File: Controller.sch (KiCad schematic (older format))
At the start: 16 parts, among them IC1 SN74HCT245PWR, J1 RGB_3_pin, J2 RGB_3_pin, J3 RGB_3_pin, J4 RGB_3_pin, J5 RGB_3_pin, J6 RGB_3_pin, J7 RGB_3_pin, J8 RGB_3_pin, J9 AMP_Mate-N-Lok_Power, U1 ESP32_DevKit_V1_DOIT

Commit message: Rename project and create manufacturing files.
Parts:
- C1: footprint Capacitor_SMD:C_0603_1608Metric_Pad1.08x0.95mm_HandSolder -> Capacitor_SMD:C_0603_1608Metric
- IC1: footprint local:SN74HCT245PWR -> Package_SO:TSSOP-20_4.4x6.5mm_P0.65mm
- J9: footprint local:TE_MATE-N-LOK_350211-1_1x04_P5.08mm_Vertical -> Connector_TE-Connectivity:TE_MATE-N-LOK_1-794374-x_1x01_P4.14mm_Horizontal
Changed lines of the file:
@@
 F 0 "J9" H 4028 1446 50  0000 L CNN
 F 1 "AMP_Mate-N-Lok_Power" H 4028 1355 50  0000 L CNN
-F 2 "local:TE_MATE-N-LOK_350211-1_1x04_P5.08mm_Vertical" H 4050 1650 50  0001 L CNN
+F 2 "Connector_TE-Connectivity:TE_MATE-N-LOK_1-794374-x_1x01_P4.14mm_Horizontal" H 4050 1650 50  0001 L CNN
 F 3 "http://uk.rs-online.com/web/p/products/0471430" H 4050 1550 50  0001 L CNN
 F 4 "Pin & Socket Connectors CONN PCM 4 POS TIN" H 4050 1450 50  0001 L CNN "Description"
@@
 F 0 "C1" V 3921 3950 50  0000 C CNN
 F 1 "100nF" V 4012 3950 50  0000 C CNN
-F 2 "Capacitor_SMD:C_0603_1608Metric_Pad1.08x0.95mm_HandSolder" H 4150 3950 50  0001 C CNN
+F 2 "Capacitor_SMD:C_0603_1608Metric" H 4150 3950 50  0001 C CNN
 F 3 "~" H 4150 3950 50  0001 C CNN
 	1    4150 3950
@@
 Wire Wire Line
 	4650 4050 4650 4400
-Wire Bus Line
-	5000 2800 5000 5800
-Wire Bus Line
-	3250 3850 3250 5700
 $Comp
 L local:SN74HCT245PWR IC1
@@
 F 0 "IC1" H 4150 4665 50  0000 C CNN
 F 1 "SN74HCT245PWR" H 4150 4574 50  0000 C CNN
-F 2 "local:SN74HCT245PWR" H 4500 4500 50  0001 L CNN
+F 2 "Package_SO:TSSOP-20_4.4x6.5mm_P0.65mm" H 4500 4500 50  0001 L CNN
 F 3 "http://www.ti.com/general/docs/suppproductinfo.tsp?distId=10&gotoUrl=http%3A%2F%2Fwww.ti.com%2Flit%2Fgpn%2Fsn74hct245" H 4500 4400 50  0001 L CNN
 F 4 "Octal Bus Transceivers With 3-State Outputs" H 4500 4300 50  0001 L CNN "Description"
@@
 	1    0    0    -1
 $EndComp
+Wire Bus Line
+	5000 2800 5000 5800
+Wire Bus Line
+	3250 3850 3250 5700
 $EndSCHEMATC

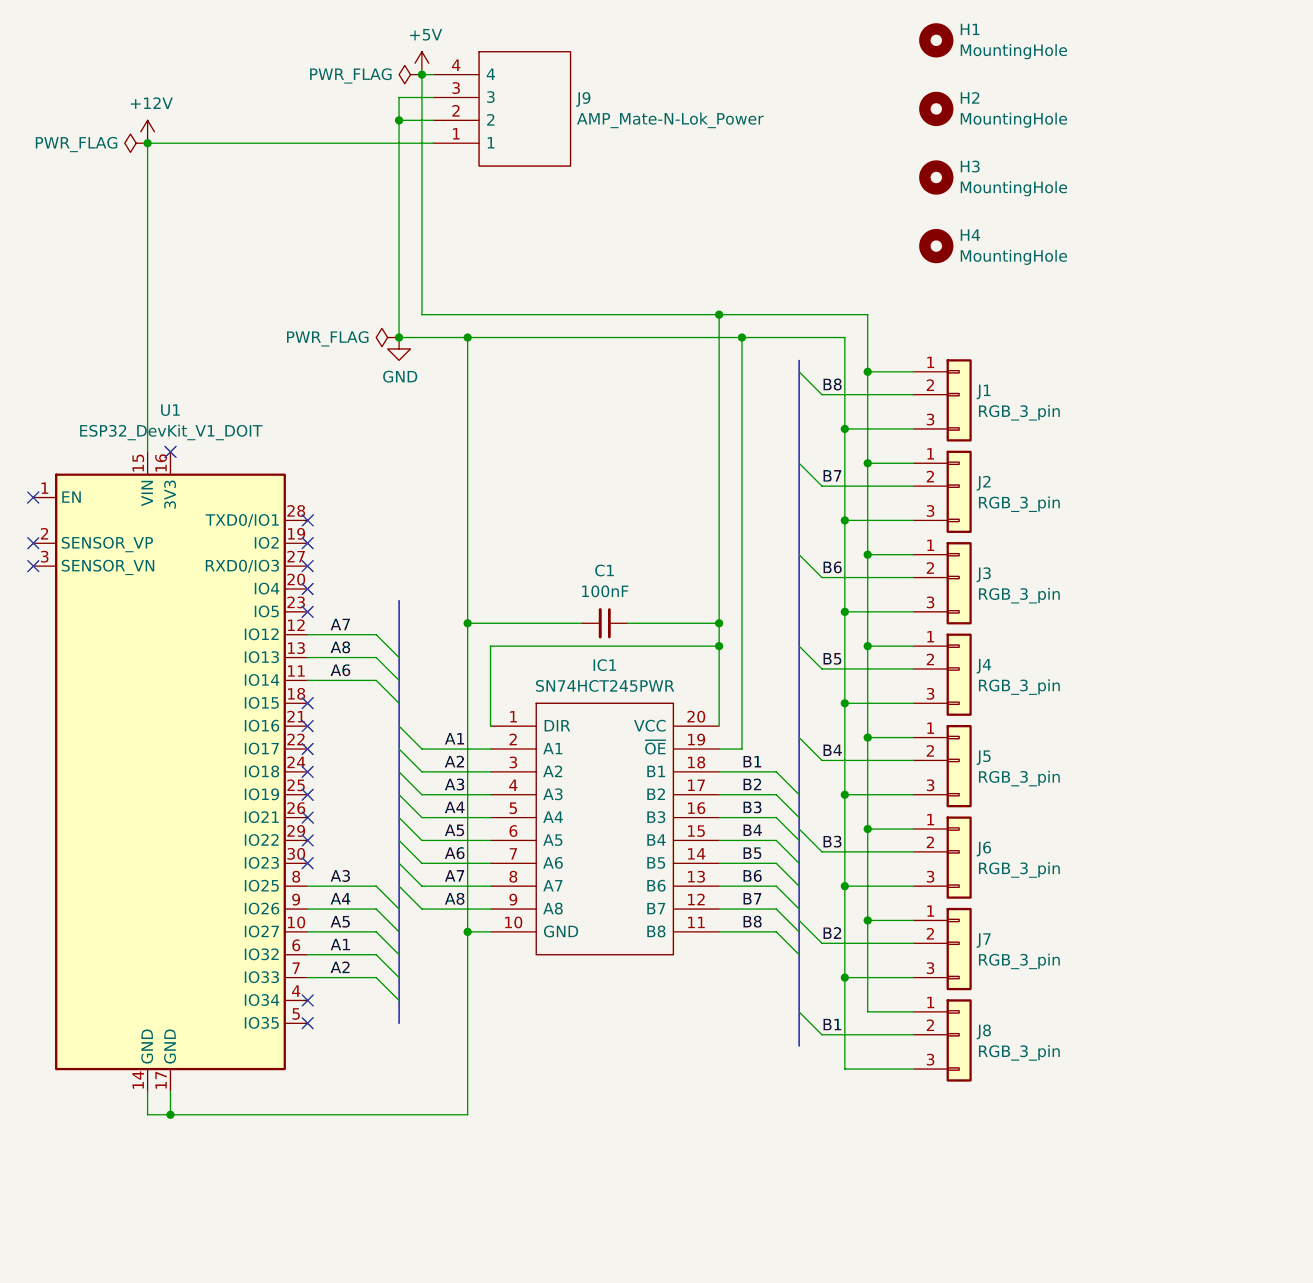
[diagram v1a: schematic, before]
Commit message: More compact layout with 10 channels.
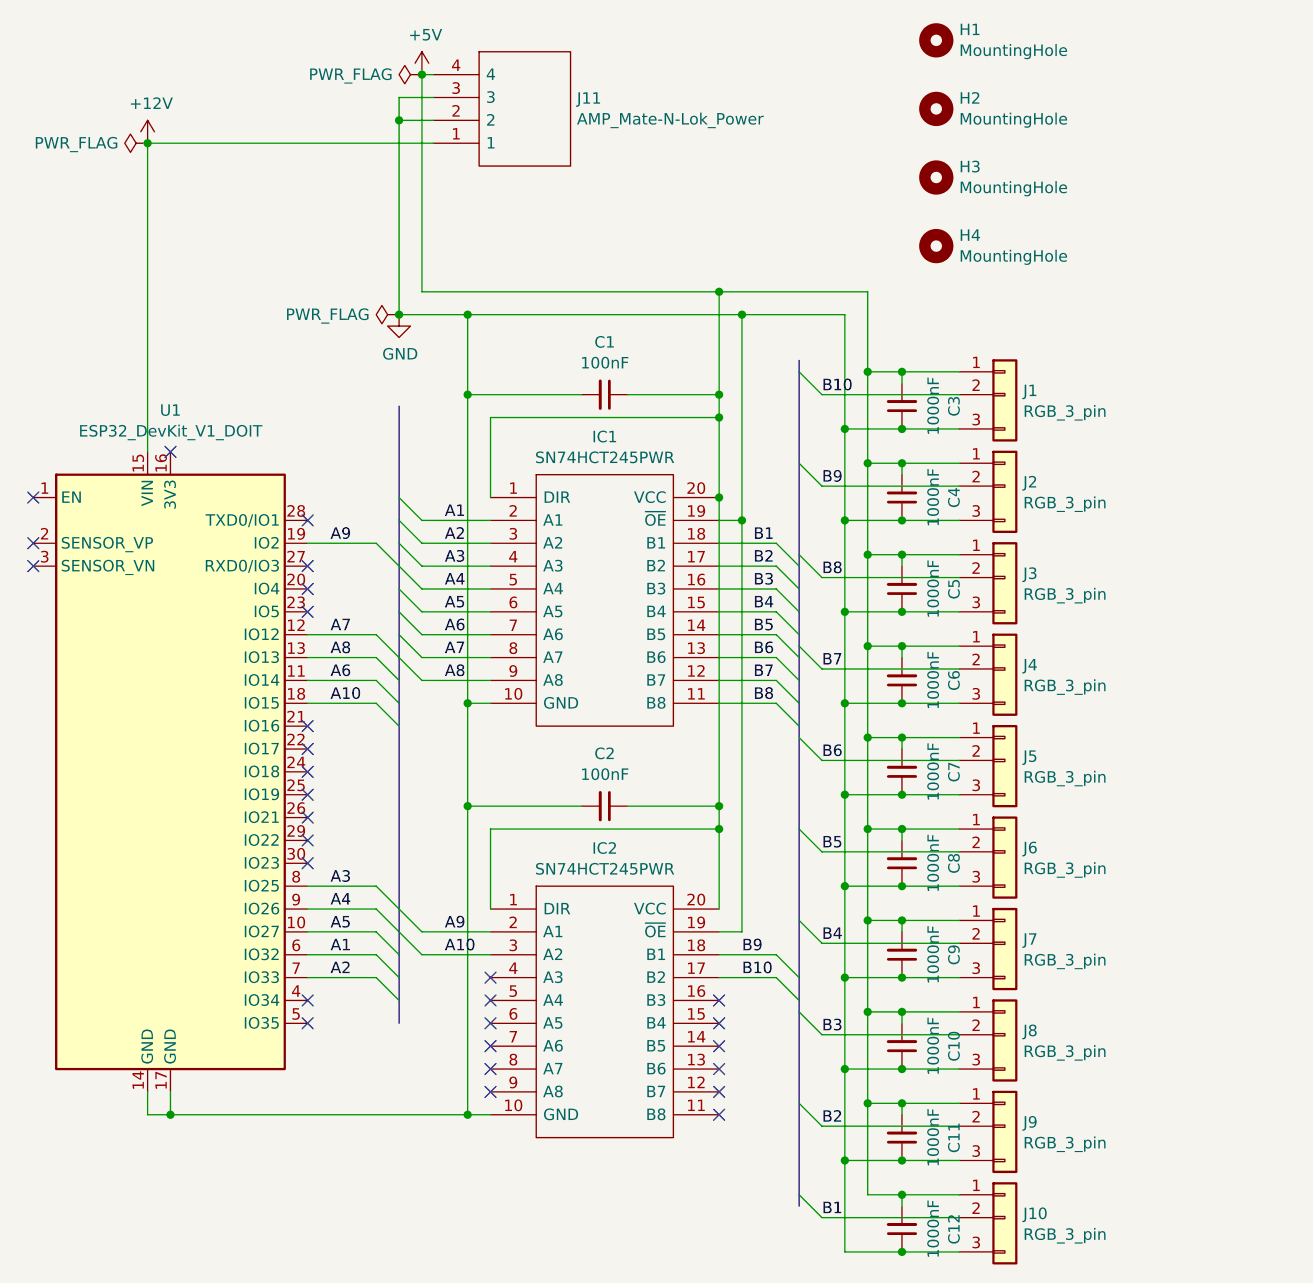
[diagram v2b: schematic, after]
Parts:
- added C10, C11, C12, C3, C4, C5, C6, C7, C8, C9: 1000nF, Capacitor_SMD:C_0603_1608Metric, symbol Device:C_Small
- added C2: 100nF, Capacitor_SMD:C_0603_1608Metric, symbol Device:C_Small
- added IC2: SN74HCT245PWR, Package_SO:TSSOP-20_4.4x6.5mm_P0.65mm, symbol local:SN74HCT245PWR
- added J10, J9: RGB_3_pin, local:RGB_3-Pin, symbol local:RGB_3_pin
- renumbered J9 to J11
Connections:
- net +5V: now also C10.2, C11.2, C12.2, C2.1, C3.2, C4.2, C5.2, C6.2, C7.2, C8.2, C9.2, IC2.1 (DIR), IC2.20 (VCC), J10.1 (Pin_1), J9.1 (Pin_1)
- net B1: now also J10.2 (Pin_2); no longer J8.2 (Pin_2)
- net B2: now also J9.2 (Pin_2); no longer J7.2 (Pin_2)
- net B3: now also J8.2 (Pin_2); no longer J6.2 (Pin_2)
- net B4: now also J7.2 (Pin_2); no longer J5.2 (Pin_2)
- net B5: now also J6.2 (Pin_2); no longer J4.2 (Pin_2)
- net B6: now also J5.2 (Pin_2); no longer J3.2 (Pin_2)
- net B7: now also J4.2 (Pin_2); no longer J2.2 (Pin_2)
- net B8: now also J3.2 (Pin_2); no longer J1.2 (Pin_2)
- net GND: now also C10.1, C11.1, C12.1, C2.2, C3.1, C4.1, C5.1, C6.1, C7.1, C8.1, C9.1, IC2.10 (GND), IC2.19 (~OE), J10.3 (Pin_3), J9.3 (Pin_3)
- net A10: now reaches U1.18 (IO15)
- net A10: now also IC2.3 (A2)
- net A9: now reaches U1.19 (IO2)
- net A9: now also IC2.2 (A1)
- new net B10: IC2.17 (B2), J1.2 (Pin_2)
- new net B9: IC2.18 (B1), J2.2 (Pin_2)
- no-connect marks 19 -> 29
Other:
- moved on the sheet: C1, IC1, J1, J2, J3, J4, J5, J6, J7, J8

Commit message: Update controller to new design.
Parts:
- removed C10, C11, C12, C5, C6, C7, C8, C9: 1000nF, Capacitor_SMD:C_0603_1608Metric, symbol Device:C_Small
- added H5, H6: MountingHole, local:ToolingHole_1.152mm, symbol Mechanical:MountingHole
- C3: value 1000nF -> 100nF
- C4: value 1000nF -> 47uF
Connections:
- net +5V: now also C4.1, U1.15 (VIN); no longer C4.2
- net GND: now also C4.2; no longer C4.1
- net +12V: no longer names the net of J11.1
- net +12V: no longer U1.15 (VIN)
- no-connect marks 29 -> 30
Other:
- moved on the sheet: J1, J10, J2, J3, J4, J5, J6, J7, J8, J9, U1

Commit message: Use 47uF capacitor which is available in JLC's basic library.
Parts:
- C4: footprint Capacitor_SMD:C_0603_1608Metric -> Capacitor_SMD:C_1206_3216Metric
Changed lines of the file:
@@
 F 0 "C4" V 2521 2900 50  0000 C CNN
 F 1 "47uF" V 2612 2900 50  0000 C CNN
-F 2 "Capacitor_SMD:C_0603_1608Metric" H 2750 2900 50  0001 C CNN
+F 2 "Capacitor_SMD:C_1206_3216Metric" H 2750 2900 50  0001 C CNN
 F 3 "~" H 2750 2900 50  0001 C CNN
 	1    2750 2900
@@
 	2650 2800 2850 2800
 NoConn ~ 3400 1850
-Wire Bus Line
-	5000 2800 5000 6500
-Wire Bus Line
-	3250 3000 3250 5700
 $Comp
 L Mechanical:MountingHole H5
@@
 	1    0    0    -1
 $EndComp
+Wire Bus Line
+	5000 2800 5000 6500
+Wire Bus Line
+	3250 3000 3250 5700
 $EndSCHEMATC
